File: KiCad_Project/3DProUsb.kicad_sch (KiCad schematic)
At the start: 25 parts

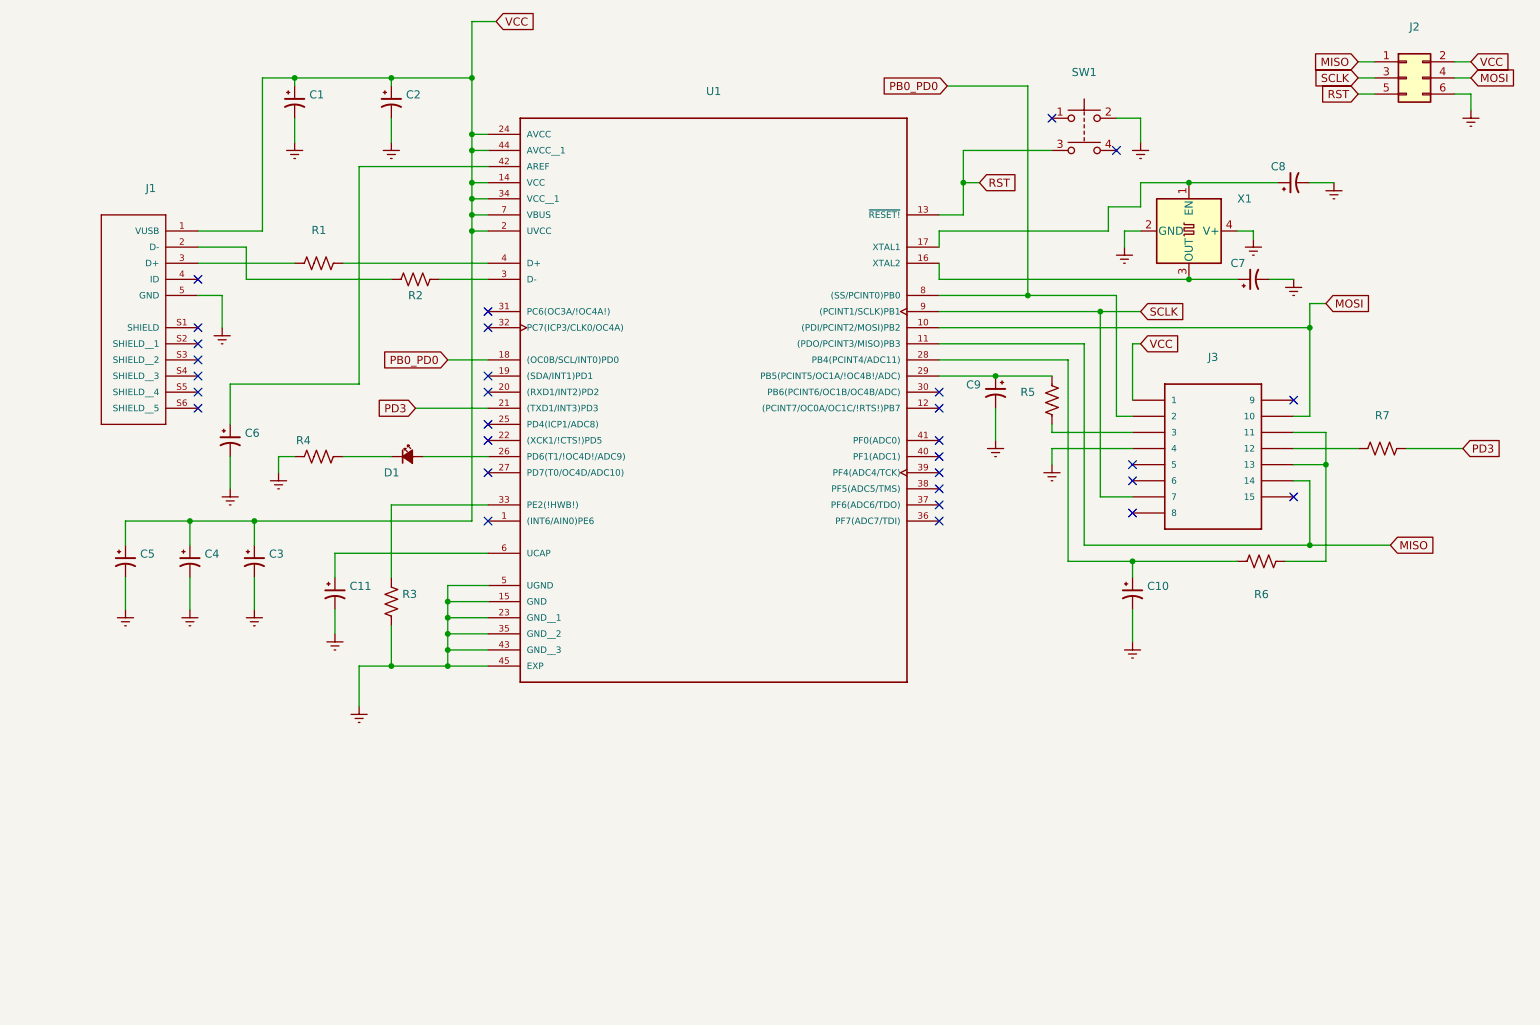
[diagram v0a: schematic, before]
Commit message: Initial USB C revision
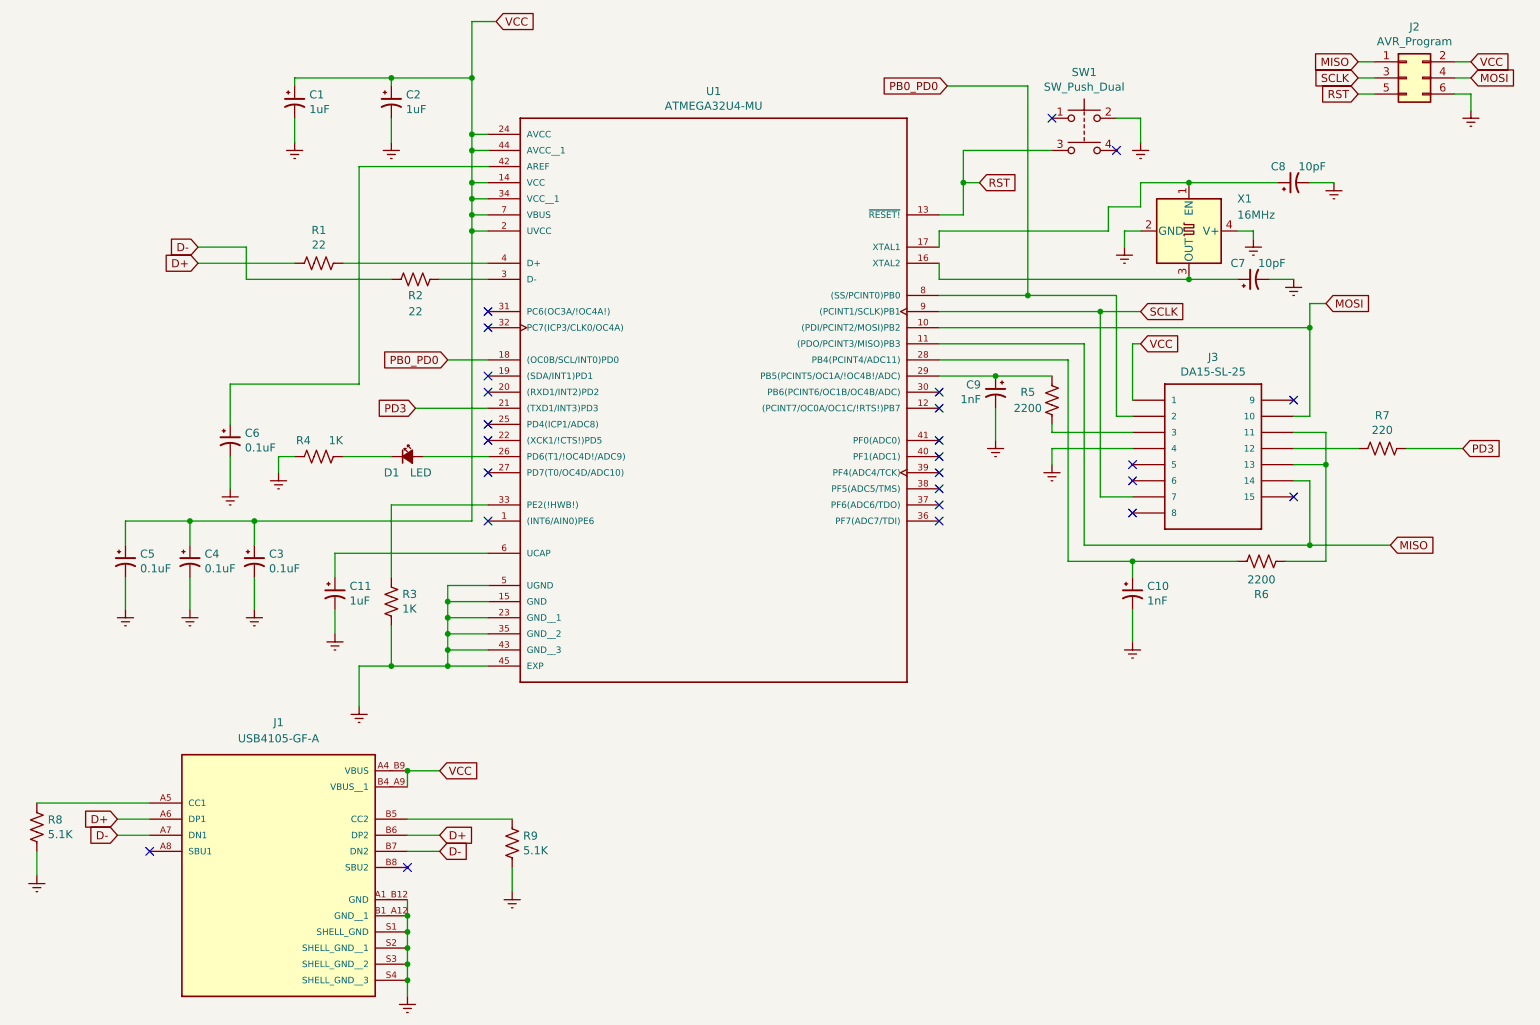
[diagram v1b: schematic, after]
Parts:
- removed J1: (no value), symbol USB:10118193-0001LF
- added J1: USB4105-GF-A, GCT_USB4105-GF-A, symbol USB4105-GF-A:USB4105-GF-A
- added R8, R9: 5.1K, Resistor_SMD:R_0402_1005Metric, symbol Device:R_US
- C1, C11, C2: value (none) -> 1uF; footprint (none) -> Capacitor_SMD:C_0402_1005Metric
- C10, C9: value (none) -> 1nF; footprint (none) -> Capacitor_SMD:C_0402_1005Metric
- C3, C4, C5, C6: value (none) -> 0.1uF; footprint (none) -> Capacitor_SMD:C_0402_1005Metric
- C7, C8: value (none) -> 10pF; footprint (none) -> Capacitor_SMD:C_0402_1005Metric
- D1: value (none) -> LED; footprint (none) -> LED_SMD:LED_0603_1608Metric
- J2: value (none) -> AVR_Program; footprint (none) -> TagConnect:TAG_TC2030-IDC-NL
- J3: value (none) -> DA15-SL-25; footprint (none) -> Gameport:ADAM_TECH_DA15-SL-25
- R1, R2: value (none) -> 22; footprint (none) -> Resistor_SMD:R_0402_1005Metric
- R3, R4: value (none) -> 1K; footprint (none) -> Resistor_SMD:R_0402_1005Metric
- R5, R6: value (none) -> 2200; footprint (none) -> Resistor_SMD:R_0402_1005Metric
- R7: value (none) -> 220; footprint (none) -> Resistor_SMD:R_1206_3216Metric
- SW1: value (none) -> SW_Push_Dual; footprint (none) -> Button_Switch_SMD:SW_SPST_Omron_B3FS-100xP
- U1: value (none) -> ATMEGA32U4-MU; footprint (none) -> Atmel:QFN50P700X700X100-45N
- X1: value (none) -> 16MHz; footprint (none) -> Oscillator:Oscillator_SMD_SeikoEpson_SG8002CE-4Pin_3.2x2.5mm
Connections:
- net Earth: now also J1.A1_B12 (GND), J1.B1_A12 (GND__1), J1.S1 (SHELL_GND), J1.S2 (SHELL_GND__1), J1.S3 (SHELL_GND__2), J1.S4 (SHELL_GND__3), R8.2, R9.2
- net VCC: now also J1.A4_B9 (VBUS), J1.B4_A9 (VBUS__1)
- net D+: now reaches R1.2
- net D+: now also J1.A6 (DP1), J1.B6 (DP2)
- net D-: now reaches R2.2
- net D-: now also J1.A7 (DN1), J1.B7 (DN2)
- new net: J1.B5 (CC2), R9.1
- new net: J1.A5 (CC1), R8.1
- no-connect marks 30 -> 25

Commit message: Don't cut the ground plane from under the USB pair
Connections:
- net D+: no longer J1.B6 (DP2), R1.2
- net D-: no longer J1.B7 (DN2), R2.2
- net 32U4_D+: now reaches R1.1, U1.4 (D+)
- net 32U4_D-: now reaches R2.1, U1.3 (D-)
- new net USB_D+: J1.B6 (DP2), R1.2
- new net USB_D-: J1.B7 (DN2), R2.2
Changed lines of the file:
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@@
   (junction (at 162.56 69.85) (diameter 0) (color 0 0 0 0)
   )
+  (junction (at 80.01 85.09) (diameter 0) (color 0 0 0 0)
+  )
   (junction (at 81.28 135.89) (diameter 0) (color 0 0 0 0)
   )
@@
   )
   (junction (at 85.09 72.39) (diameter 0) (color 0 0 0 0)
+  )
+  (junction (at 80.01 82.55) (diameter 0) (color 0 0 0 0)
   )
   (junction (at 74.93 190.5) (diameter 0) (color 0 0 0 0)
@@
     (stroke (width 0) (type default) (color 0 0 0 0))
   )
-  (wire (pts (xy 64.77 82.55) (xy 87.63 82.55))
+  (wire (pts (xy 64.77 82.55) (xy 80.01 82.55))
     (stroke (width 0) (type default) (color 0 0 0 0))
   )
@@
     (stroke (width 0) (type default) (color 0 0 0 0))
   )
+  (wire (pts (xy 78.74 92.71) (xy 80.01 92.71))
+    (stroke (width 0) (type default) (color 0 0 0 0))
+  )
   (wire (pts (xy 162.56 64.77) (xy 176.53 64.77))
     (stroke (width 0) (type default) (color 0 0 0 0))
   )
+  (wire (pts (xy 80.01 82.55) (xy 87.63 82.55))
+    (stroke (width 0) (type default) (color 0 0 0 0))
+  )
   (wire (pts (xy 189.23 95.25) (xy 189.23 104.14))
     (stroke (width 0) (type default) (color 0 0 0 0))
@@
     (stroke (width 0) (type default) (color 0 0 0 0))
   )
+  (wire (pts (xy 78.74 80.01) (xy 80.01 80.01))
+    (stroke (width 0) (type default) (color 0 0 0 0))
+  )
   (wire (pts (xy 189.23 111.76) (xy 176.53 111.76))
     (stroke (width 0) (type default) (color 0 0 0 0))
@@
     (stroke (width 0) (type default) (color 0 0 0 0))
   )
+  (wire (pts (xy 80.01 80.01) (xy 80.01 82.55))
+    (stroke (width 0) (type default) (color 0 0 0 0))
+  )
   (wire (pts (xy 87.63 113.03) (xy 77.47 113.03))
     (stroke (width 0) (type default) (color 0 0 0 0))
@@
   )
   (wire (pts (xy 72.39 59.69) (xy 72.39 63.5))
+    (stroke (width 0) (type default) (color 0 0 0 0))
+  )
+  (wire (pts (xy 80.01 92.71) (xy 80.01 85.09))
     (stroke (width 0) (type default) (color 0 0 0 0))
   )
@@
     )
   )
-  (global_label "D+" (shape input) (at 41.91 82.55 180) (fields_autoplaced)
+  (global_label "USB_D+" (shape input) (at 41.91 82.55 180) (fields_autoplaced)
     (effects (font (size 1.27 1.27)) (justify right))
-    (property "Intersheet References" "${INTERSHEET_REFS}" (id 0) (at 36.7434 82.4706 0)
+    (property "Intersheet References" "${INTERSHEET_REFS}" (id 0) (at 31.9658 82.4706 0)
       (effects (font (size 1.27 1.27)) (justify right) hide)
     )
   )
-  (global_label "D+" (shape input) (at 80.01 172.72 0) (fields_autoplaced)
+  (global_label "USB_D+" (shape input) (at 80.01 172.72 0) (fields_autoplaced)
     (effects (font (size 1.27 1.27)) (justify left))
-    (property "Intersheet References" "${INTERSHEET_REFS}" (id 0) (at 85.1766 172.6406 0)
+    (property "Intersheet References" "${INTERSHEET_REFS}" (id 0) (at 89.9542 172.6406 0)
       (effects (font (size 1.27 1.27)) (justify left) hide)
     )
@@
     )
   )
-  (global_label "D-" (shape input) (at 41.91 80.01 180) (fields_autoplaced)
+  (global_label "USB_D-" (shape input) (at 41.91 80.01 180) (fields_autoplaced)
     (effects (font (size 1.27 1.27)) (justify right))
-    (property "Intersheet References" "${INTERSHEET_REFS}" (id 0) (at 36.7434 79.9306 0)
+    (property "Intersheet References" "${INTERSHEET_REFS}" (id 0) (at 31.9658 79.9306 0)
       (effects (font (size 1.27 1.27)) (justify right) hide)
     )
@@
     )
   )
+  (global_label "32U4_D+" (shape input) (at 78.74 80.01 180) (fields_autoplaced)
+    (effects (font (size 1.27 1.27)) (justify right))
+    (property "Intersheet References" "${INTERSHEET_REFS}" (id 0) (at 67.6468 79.9306 0)
+      (effects (font (size 1.27 1.27)) (justify right) hide)
+    )
+  )
   (global_label "PD3" (shape input) (at 241.3 111.76 0) (fields_autoplaced)
     (effects (font (size 1.27 1.27)) (justify left))
@@
     )
   )
-  (global_label "D-" (shape input) (at 80.01 175.26 0) (fields_autoplaced)
+  (global_label "USB_D-" (shape input) (at 80.01 175.26 0) (fields_autoplaced)
     (effects (font (size 1.27 1.27)) (justify left))
-    (property "Intersheet References" "${INTERSHEET_REFS}" (id 0) (at 85.1766 175.1806 0)
+    (property "Intersheet References" "${INTERSHEET_REFS}" (id 0) (at 89.9542 175.1806 0)
       (effects (font (size 1.27 1.27)) (justify left) hide)
+    )
+  )
+  (global_label "32U4_D-" (shape input) (at 78.74 92.71 180) (fields_autoplaced)
+    (effects (font (size 1.27 1.27)) (justify right))
+    (property "Intersheet References" "${INTERSHEET_REFS}" (id 0) (at 67.6468 92.6306 0)
+      (effects (font (size 1.27 1.27)) (justify right) hide)
     )
   )
@@
   (symbol (lib_id "power:Earth") (at 187.96 80.01 0) (unit 1)
     (in_bom yes) (on_board yes)
-    (property "Reference" "#PWR?" (id 0) (at 187.96 86.36 0)
+    (property "Reference" "#PWR0120" (id 0) (at 187.96 86.36 0)
       (effects (font (size 1.27 1.27)) hide)
     )
@@
   (symbol (lib_id "power:Earth") (at 208.28 78.74 0) (unit 1)
     (in_bom yes) (on_board yes)
-    (property "Reference" "#PWR?" (id 0) (at 208.28 85.09 0)
+    (property "Reference" "#PWR0121" (id 0) (at 208.28 85.09 0)
       (effects (font (size 1.27 1.27)) hide)
     )
@@
   (symbol (lib_id "power:Earth") (at 63.5 140.97 0) (unit 1)
     (in_bom yes) (on_board yes)
-    (property "Reference" "#PWR?" (id 0) (at 63.5 147.32 0)
+    (property "Reference" "#PWR0101" (id 0) (at 63.5 147.32 0)
       (effects (font (size 1.27 1.27)) hide)
     )
@@
   (symbol (lib_id "power:Earth") (at 91.44 181.61 0) (unit 1)
     (in_bom yes) (on_board yes)
-    (property "Reference" "#PWR?" (id 0) (at 91.44 187.96 0)
+    (property "Reference" "#PWR0117" (id 0) (at 91.44 187.96 0)
       (effects (font (size 1.27 1.27)) hide)
     )
@@
   (symbol (lib_id "power:Earth") (at 74.93 198.12 0) (unit 1)
     (in_bom yes) (on_board yes)
-    (property "Reference" "#PWR?" (id 0) (at 74.93 204.47 0)
+    (property "Reference" "#PWR0118" (id 0) (at 74.93 204.47 0)
       (effects (font (size 1.27 1.27)) hide)
     )
@@
   (symbol (lib_id "power:Earth") (at 16.51 179.07 0) (unit 1)
     (in_bom yes) (on_board yes)
-    (property "Reference" "#PWR?" (id 0) (at 16.51 185.42 0)
+    (property "Reference" "#PWR0119" (id 0) (at 16.51 185.42 0)
       (effects (font (size 1.27 1.27)) hide)
     )
@@
   )
   (symbol_instances
+    (path "/00000000-0000-0000-0000-00005f93972c"
+      (reference "#PWR0101") (unit 1) (value "Earth") (footprint "")
+    )
     (path "/00000000-0000-0000-0000-00005f4a33c9"
       (reference "#PWR0102") (unit 1) (value "Earth") (footprint "")
@@
       (reference "#PWR0116") (unit 1) (value "Earth") (footprint "")
     )
+    (path "/184e9d0c-ac5d-4828-9e1d-20b2e3f46a80"
+      (reference "#PWR0117") (unit 1) (value "Earth") (footprint "")
+    )
+    (path "/5ec2f63c-add6-499c-b53e-7424c5c6db66"
+      (reference "#PWR0118") (unit 1) (value "Earth") (footprint "")
+    )
+    (path "/b0b6b5c4-fe9d-4bf0-9e04-2c00d045e80f"
+      (reference "#PWR0119") (unit 1) (value "Earth") (footprint "")
+    )
     (path "/00000000-0000-0000-0000-00005f6d414b"
-      (reference "#PWR?") (unit 1) (value "Earth") (footprint "")
+      (reference "#PWR0120") (unit 1) (value "Earth") (footprint "")
     )
     (path "/00000000-0000-0000-0000-00005f6d5453"
-      (reference "#PWR?") (unit 1) (value "Earth") (footprint "")
-    )
-    (path "/00000000-0000-0000-0000-00005f93972c"
-      (reference "#PWR?") (unit 1) (value "Earth") (footprint "")
-    )
-    (path "/184e9d0c-ac5d-4828-9e1d-20b2e3f46a80"
-      (reference "#PWR?") (unit 1) (value "Earth") (footprint "")
-    )
-    (path "/5ec2f63c-add6-499c-b53e-7424c5c6db66"
-      (reference "#PWR?") (unit 1) (value "Earth") (footprint "")
-    )
-    (path "/b0b6b5c4-fe9d-4bf0-9e04-2c00d045e80f"
-      (reference "#PWR?") (unit 1) (value "Earth") (footprint "")
+      (reference "#PWR0121") (unit 1) (value "Earth") (footprint "")
     )
     (path "/00000000-0000-0000-0000-00005f4a274e"

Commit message: Revised layout
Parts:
- SW1: symbol Switch:SW_Push_Dual -> Switch:SW_Push
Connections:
- net D+ is gone; now on net USB_D+: J1.A6 (DP1)
- net D- is gone; now on net USB_D-: J1.A7 (DN1)
- net RST: now also SW1.1; no longer SW1.3
- no-connect marks 25 -> 23
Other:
- moved on the sheet: R8
